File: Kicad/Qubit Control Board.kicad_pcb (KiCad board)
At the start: 6 copper layers, 64 x 81.5 mm, 154 parts, among them J1 USB_C_Receptacle_PowerOnly_6P, J2 CLK_Pins, J3 Idata, J4 Qdata, J5 SPIdata, J6 SMA, U1 LT3045xMSE, U2 TRF372017IRGZR, U3 LT3045xMSE, U4 LT3045xMSE, U5 SN65LVDS1DBV, U6 AD9743BCPZ, Y2 CVHD-950-100.000

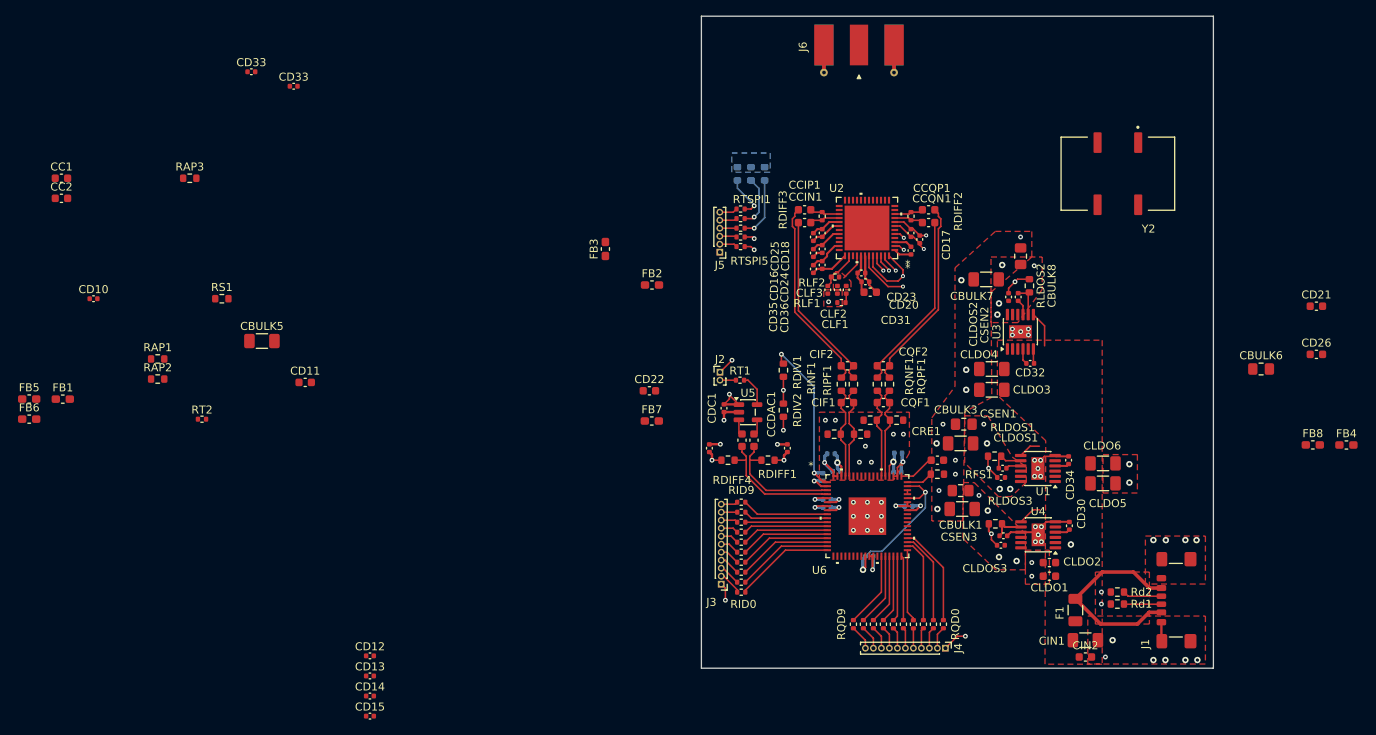
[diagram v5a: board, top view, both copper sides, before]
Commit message: REREF routing with on board clock
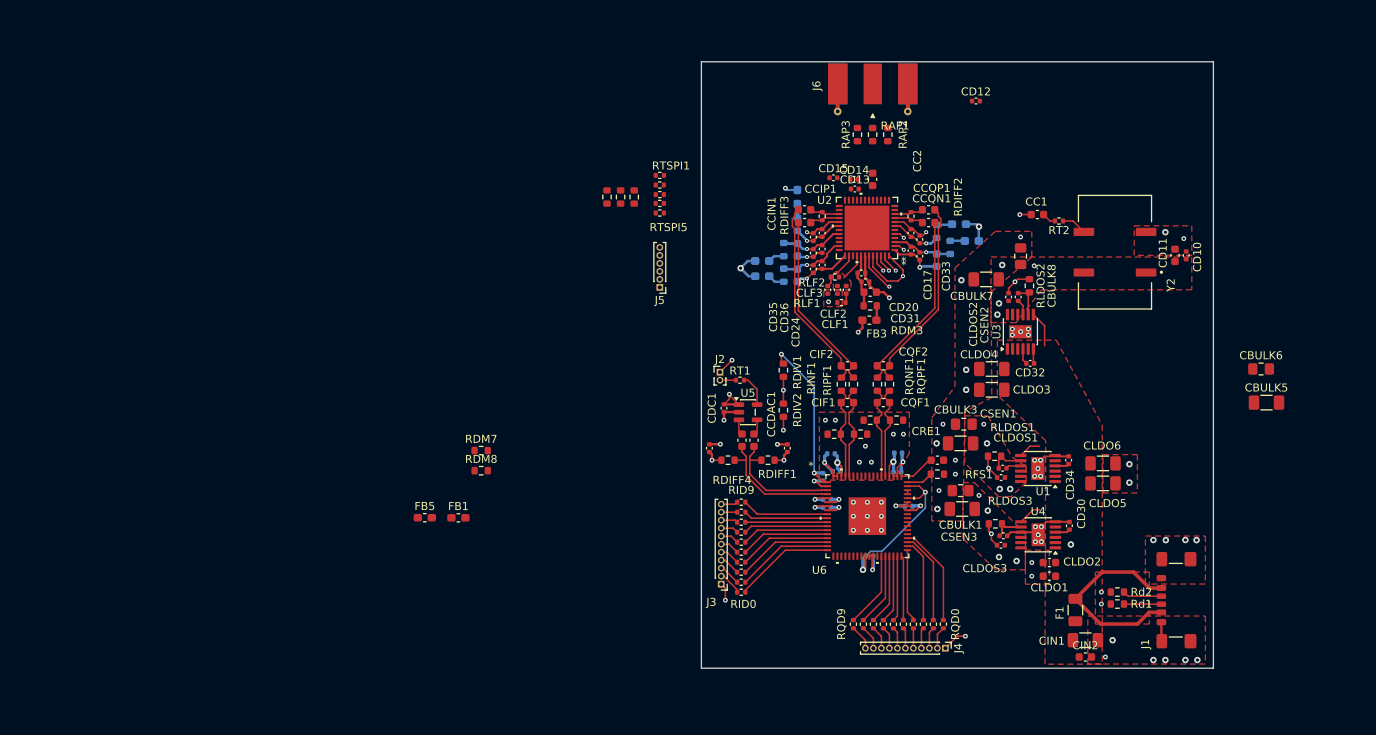
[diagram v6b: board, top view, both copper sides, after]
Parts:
- removed the CD33 at (50.2, 42.9)
- removed the CD33 at (55.5, 44.8)
- removed RS1: 0R, Resistor_SMD:R_0603_1608Metric
- added CD33: 10n, Capacitor_SMD:C_0402_1005Metric, F.Cu at (133.8, 66.0)
- added RDM1: 0R, Resistor_SMD:R_0603_1608Metric, B.Cu at (118.5, 62.0)
- added RDM2: 0R, Resistor_SMD:R_0603_1608Metric, B.Cu at (135.9, 62.9)
- added RDM3: 0R, Resistor_SMD:R_0603_1608Metric, F.Cu at (127.6, 72.2)
- added RDM4: 0R, Resistor_SMD:R_0603_1608Metric, B.Cu at (116.8, 65.2)
- added RDM5: 0R, Resistor_SMD:R_0603_1608Metric, B.Cu at (137.6, 64.9)
- added RDM6: 0R, Resistor_SMD:R_0603_1608Metric, B.Cu at (116.8, 68.4)
- added RDM7: 0R, Resistor_SMD:R_0603_1608Metric, F.Cu at (79.0, 90.3)
- added RDM8: 0R, Resistor_SMD:R_0603_1608Metric, F.Cu at (79.0, 92.8)
- CD21, CD22, CD26, FB2, FB4, FB6, FB7, FB8: moved to B.Cu
- RPD1, RPD2, RPD3: moved to F.Cu
- moved CD10 136.7 mm to (167.1, 65.9), turned to -90 degrees
- moved CBULK5 125.8 mm to (177.1, 84.3)
- moved CC1 122.1 mm to (148.5, 60.8), turned to 180 degrees
- moved FB6 118.8 mm to (138.7, 62.0), turned to 180 degrees
- moved RT2 110.0 mm to (151.2, 61.6), turned to 180 degrees
- moved CD11 109.9 mm to (165.7, 65.9), turned to -90 degrees
- moved CD12 102.7 mm to (140.8, 46.6)
- moved CC2 101.4 mm to (127.9, 56.4), turned to 90 degrees
- moved RAP2 96.2 mm to (129.8, 50.8), turned to 90 degrees
- moved RAP1 93.7 mm to (127.9, 50.8), turned to 90 degrees
- moved CD15 88.8 mm to (123.0, 56.2)
- moved CD14 88.5 mm to (125.6, 56.4)
- moved CD13 85.9 mm to (125.7, 57.6)
- moved RAP3 83.6 mm to (126.0, 50.8), turned to 90 degrees
- moved FB8 72.0 mm to (114.1, 68.5)
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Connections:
- FB1 pad 2: /VCC_D2S -> Net-(FB1-Pad2)
- FB2 pad 2: /VCC_LO2 -> Net-(FB2-Pad2)
- FB3 pad 2: /VCC_PLL -> Net-(FB3-Pad2)
- FB4 pad 2: /VCC_DIG -> Net-(FB4-Pad2)
- FB5 pad 2: /VCC_MIX -> Net-(FB5-Pad2)
- FB6 pad 2: /VCC_LO1 -> Net-(FB6-Pad2)
- FB7 pad 2: /VCC_VCO2 -> Net-(FB7-Pad2)
- FB8 pad 2: /VCC_VCO1 -> Net-(FB8-Pad2)
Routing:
- net /REFIN: track 6.70 -> 26.5 mm, vias 1 -> 2
- net GND: track 102.2 -> 114.1 mm, vias 77 -> 84
- net +3.3V-B: track 0.00 -> 11.3 mm, vias 4 -> 8
- net /CLK: track 10.1 -> 2.41 mm, vias 2 -> 1
- net /DATA: track 8.77 -> 2.26 mm, vias 2 -> 1
- net /LE: track 7.67 -> 2.27 mm, vias 2 -> 1
- net /VCC_DIG: track 2.27 -> 7.56 mm, vias 0 -> 1
- net /VCC_VCO2: track 4.01 -> 8.03 mm, vias 0 -> 1
- net /VCC_VCO1: track 4.40 -> 8.36 mm, vias 0 -> 1
- net Net-(Y2-OUT): track 0.00 -> 3.17 mm
- net /VCC_LO2: track 3.99 -> 6.55 mm, vias 0 -> 1
- net Net-(J5-Pin_6): track 2.26 -> 0.00 mm
- net Net-(J5-Pin_2): track 2.21 -> 0.00 mm
- net Net-(J5-Pin_5): track 2.17 -> 0.00 mm
- net Net-(FB8-Pad2): track 0.00 -> 2.11 mm
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- added copper zone on In4.Cu, net +3.3V-B
- removed copper zone on B.Cu, net GND
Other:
- board size 64 x 81.5 mm -> 64 x 75.8 mm

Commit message: RFOUT routing + SMA
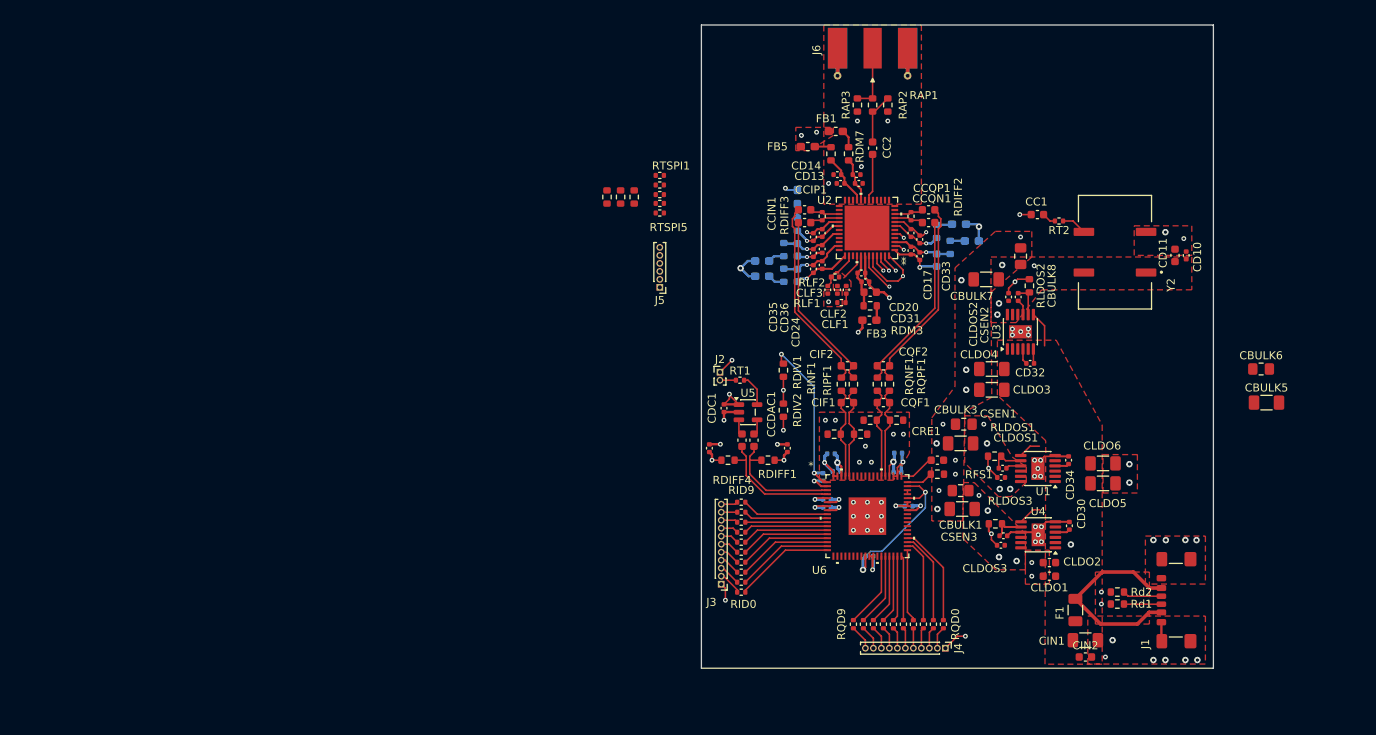
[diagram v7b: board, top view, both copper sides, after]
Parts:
- moved FB1 67.5 mm to (123.3, 50.4)
- moved FB5 66.7 mm to (119.8, 52.3)
- moved RDM7 59.0 mm to (124.9, 53.2), turned to -90 degrees
- moved RDM8 59.0 mm to (122.7, 53.2), turned to -90 degrees
- moved CD12 17.9 mm to (126.2, 56.9), turned to 180 degrees
- moved J6 4.47 mm to (127.9, 41.7)
- moved CC2 3.90 mm to (127.9, 52.5)
- moved RAP1 3.70 mm to (127.9, 47.1)
- moved RAP2 3.70 mm to (129.8, 47.1)
- moved RAP3 3.70 mm to (126.0, 47.1)
- moved CD13 1.91 mm to (123.9, 56.9)
- moved CD14 0.67 mm to (125.9, 55.8), turned to 180 degrees
- moved CD15 0.64 mm to (123.5, 55.8)
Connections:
- J6 pad 2: (no net) -> GND
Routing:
- net Net-(J6-Pin_1): track 0.00 -> 8.40 mm
- net /VCC_MIX: track 0.00 -> 6.40 mm
- net Net-(CC2-Pad2): track 0.00 -> 6.38 mm
- net /RFOUT: track 0.00 -> 5.91 mm
- net /VCC_D2S: track 0.00 -> 5.62 mm
- net Net-(FB1-Pad2): track 0.00 -> 2.28 mm
- net Net-(FB5-Pad2): track 0.00 -> 2.06 mm
- net GND: vias 84 -> 88
- net +5V: vias 1 -> 3
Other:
- board size 64 x 75.8 mm -> 64 x 80.4 mm

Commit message: SPI routing
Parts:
- RPD1, RPD2, RPD3: moved to B.Cu
- moved CBULK5 71.7 mm to (114.3, 49.8), turned to 90 degrees
- moved CBULK6 67.0 mm to (116.7, 49.8), turned to 90 degrees
- moved J5 54.6 mm to (146.3, 39.0), turned to -90 degrees
- moved RPD1 50.6 mm to (143.8, 46.2), turned to 90 degrees
- moved RTSPI5 48.3 mm to (145.7, 41.6), turned to 90 degrees
- moved RPD2 47.4 mm to (142.1, 46.2), turned to 90 degrees
- moved RTSPI4 46.7 mm to (144.5, 41.6), turned to 90 degrees
- moved RTSPI3 45.2 mm to (143.3, 41.6), turned to 90 degrees
- moved RPD3 44.1 mm to (140.4, 46.2), turned to 90 degrees
- moved RTSPI2 43.6 mm to (142.1, 41.6), turned to 90 degrees
- moved RTSPI1 42.1 mm to (140.9, 41.6), turned to 90 degrees
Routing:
- net /CLK: track 2.41 -> 35.8 mm, vias 1 -> 2
- net /LE: track 2.27 -> 35.4 mm, vias 1 -> 2
- net /DATA: track 2.26 -> 35.1 mm, vias 1 -> 2
- net /RDBK: track 1.32 -> 30.3 mm, vias 1 -> 2
- net /LD: track 1.32 -> 28.3 mm, vias 1 -> 2
- net GND: track 114.1 -> 118.3 mm, vias 88 -> 95
- net Net-(J5-Pin_6): track 0.00 -> 2.26 mm
- net Net-(J5-Pin_2): track 0.00 -> 2.26 mm
- net Net-(J5-Pin_5): track 0.00 -> 2.17 mm
- net Net-(J5-Pin_4): track 0.00 -> 2.09 mm
- net Net-(J5-Pin_3): track 0.14 -> 2.17 mm
- net +5V: vias 3 -> 4
- added copper zone on B.Cu, net GND
